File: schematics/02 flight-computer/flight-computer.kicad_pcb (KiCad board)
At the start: 2 copper layers, 186 x 186 mm, 215 parts, among them IC1 NCP4620, IC10 AD8495, IC11 AD8495, IC12 AD8656, IC13 AD8656, IC14 AD8656, IC15 AD8656, IC16 MS5611-01BA03, IC17 MPU-9250, IC18 Si4463, IC19 MAX-M8Q, IC2 STM32F405RxTx, IC20 NCP380, IC21 SN65LVDT41, IC22 MAX14787E, IC3 SL18860DC, IC4 TPS62133, IC5 ADP3335, IC6 AD8656, IC7 AD8656, IC8 AD8495, IC9 AD8495, J1 RJHSE-538x, J10 THERMO4, J11 PYRO1, J12 PYRO2, J13 PYRO_SI, J14 12V, J15 GND, J2 RJHSE-538x, J3 3V3, J4 GND, J5 PRESSURE1, J6 PRESSURE2, J7 THERMO1, J8 THERMO2, J9 THERMO3, P1 GPS, P2 TLM, P3 SWD_TC, Q1 Si5515CDC, Q2 Si5515CDC, Y1 TCXO

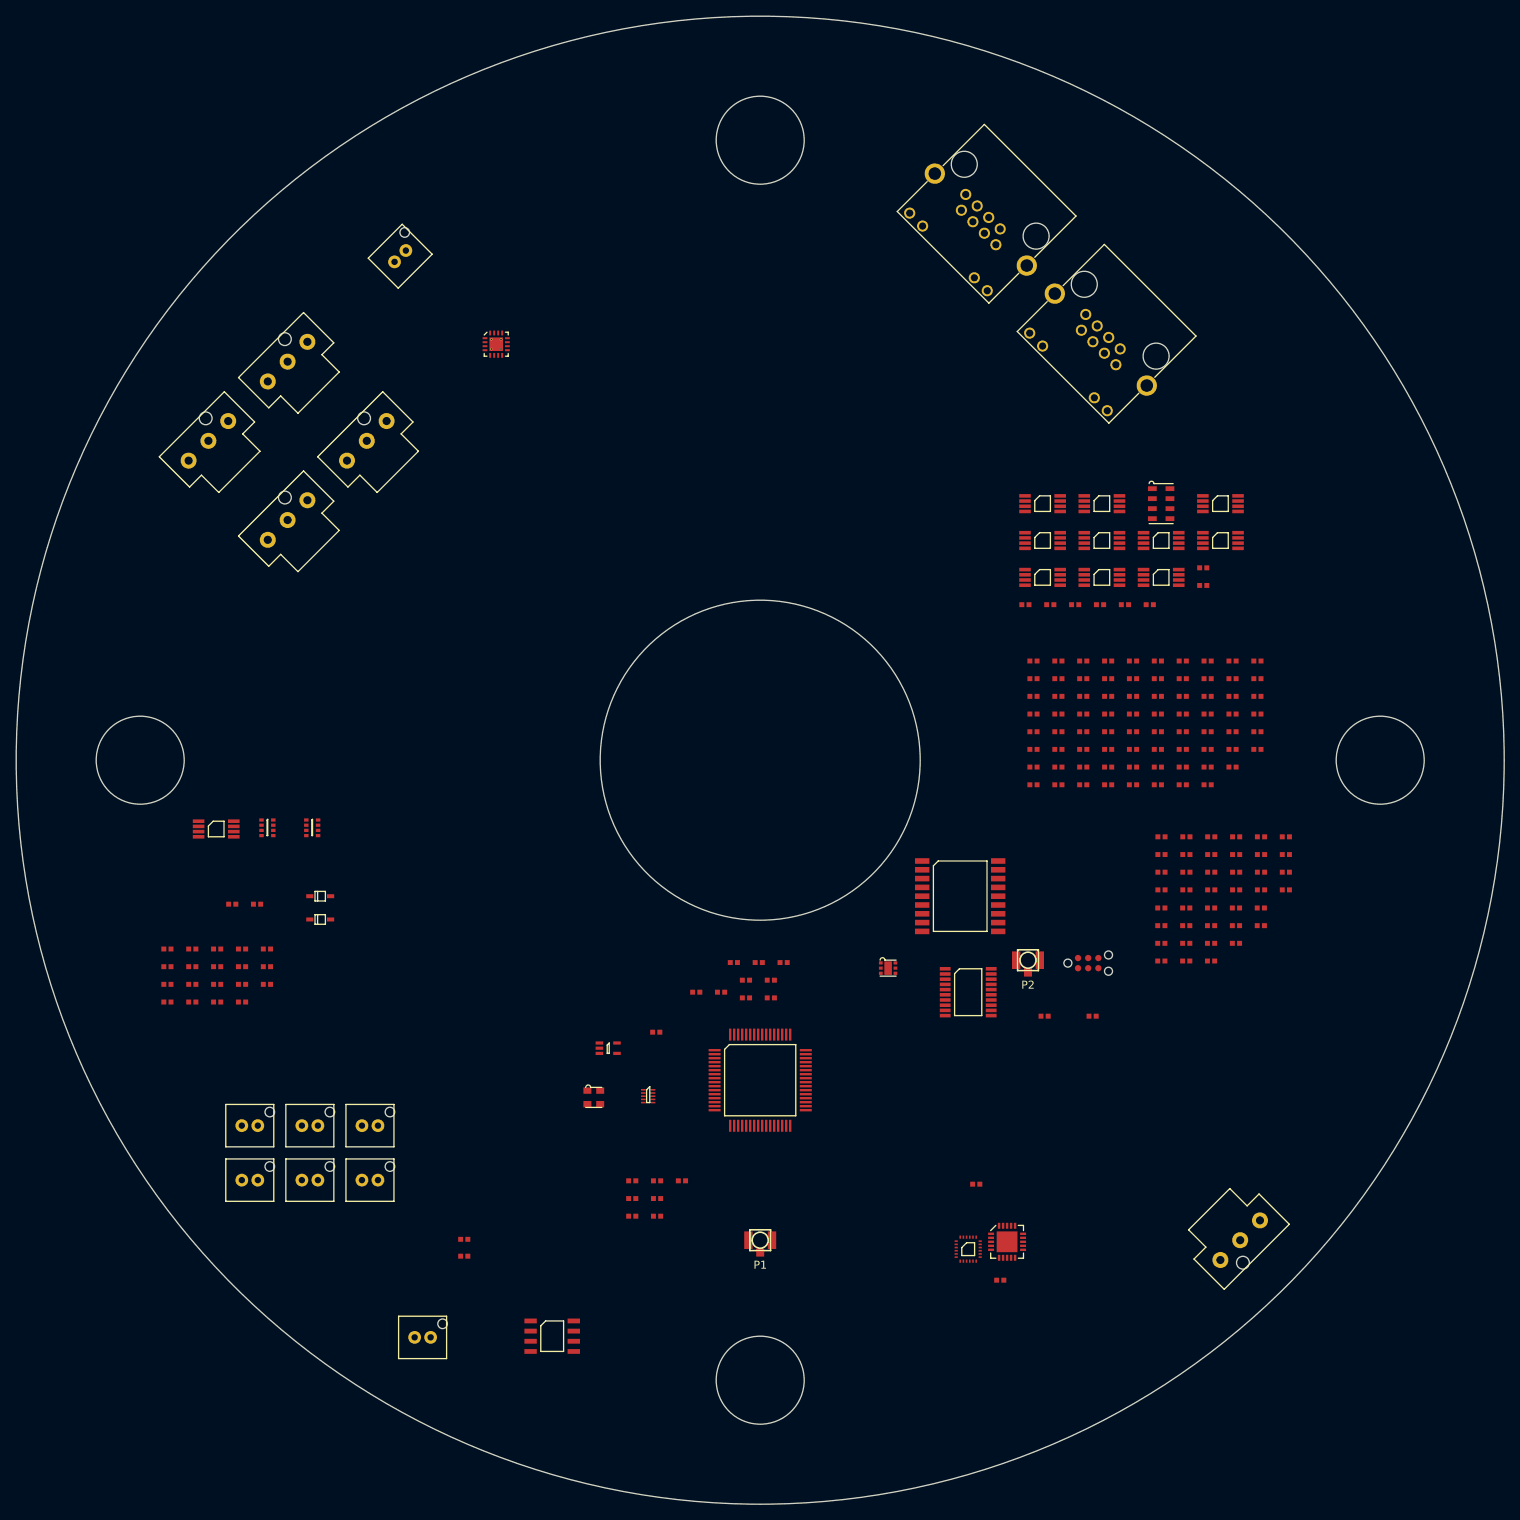
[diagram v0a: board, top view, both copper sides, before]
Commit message: Add preliminary pcb edges
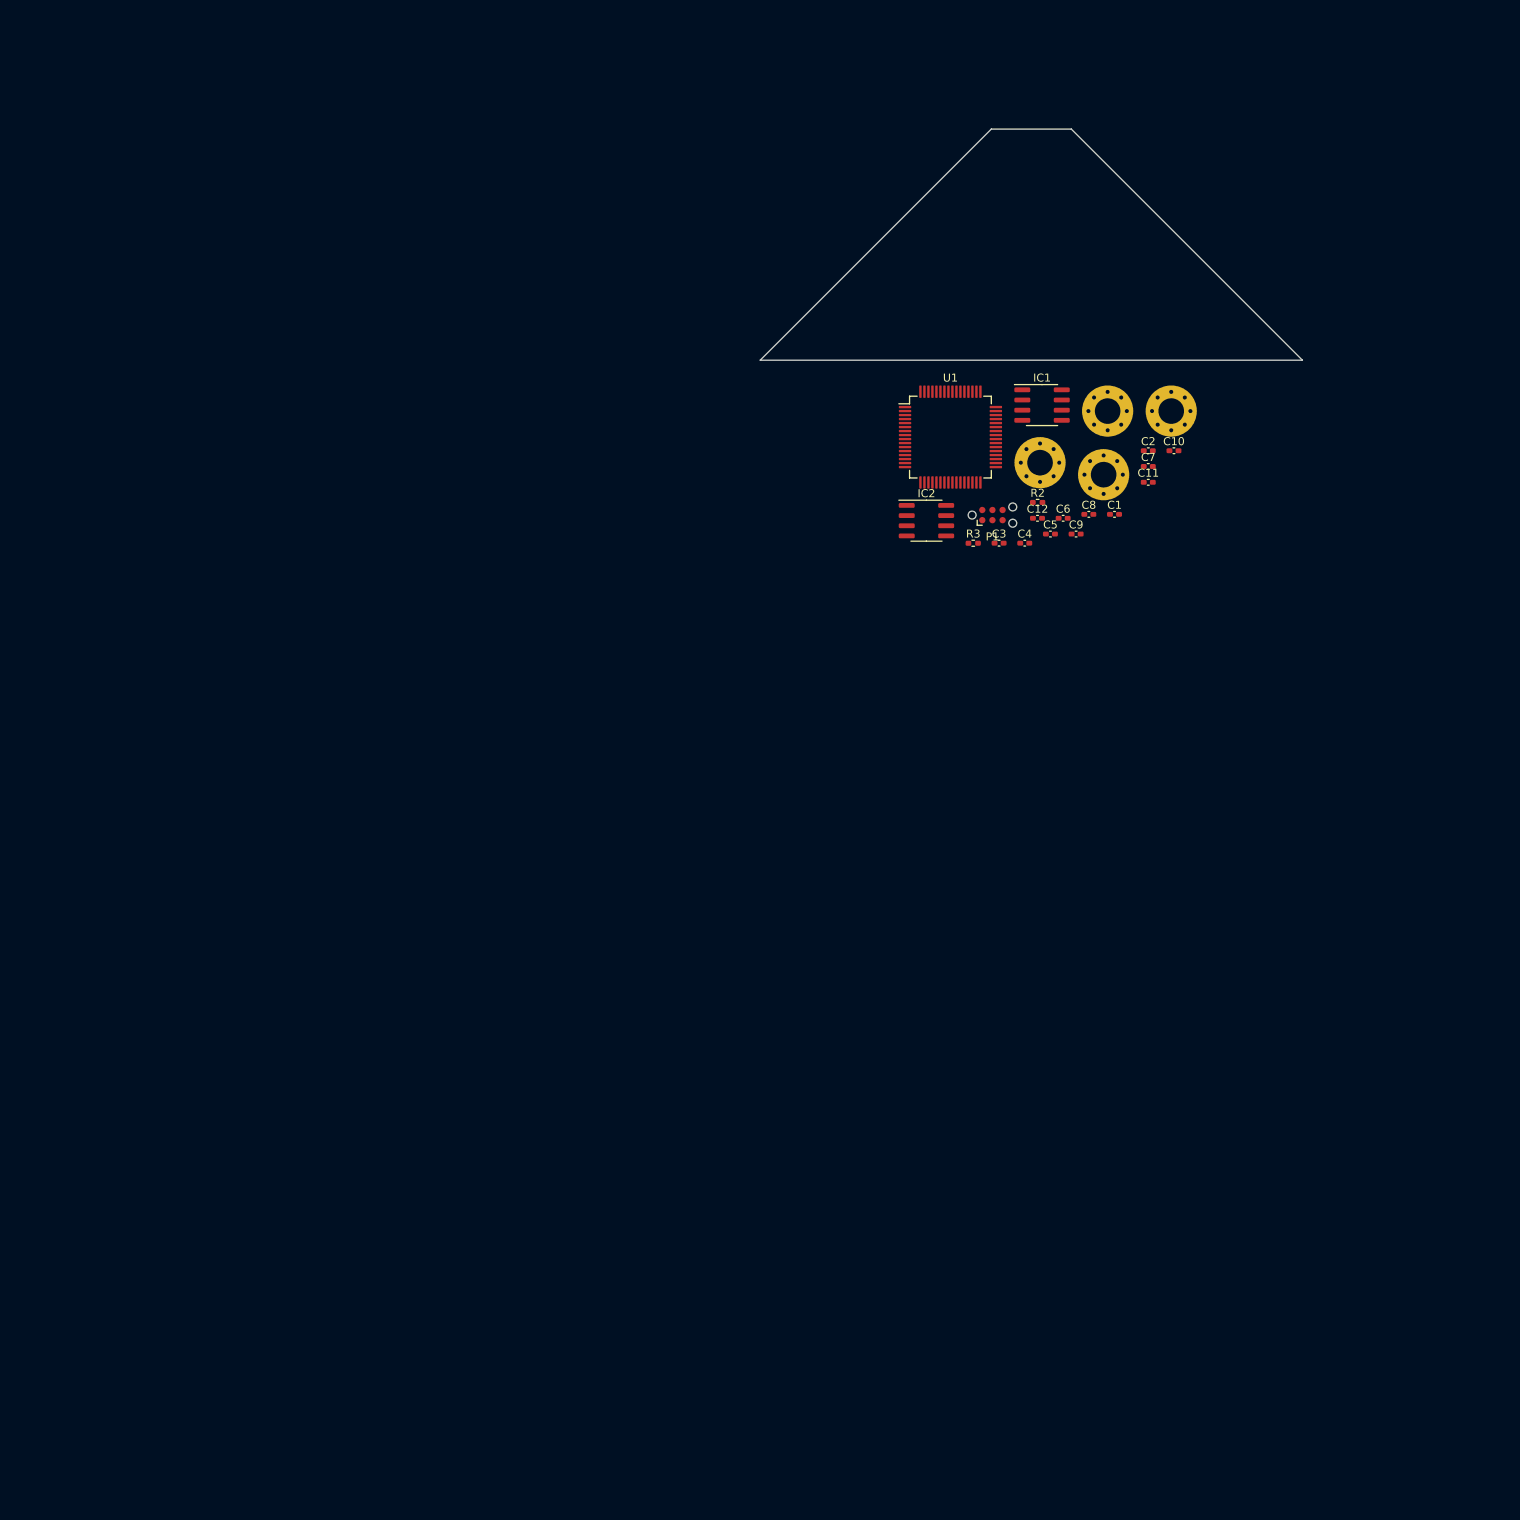
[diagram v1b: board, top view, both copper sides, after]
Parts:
- removed C13, C16, C17, C19, C20, C36, C37, C38, C39, C40, C41, C42, C43, C44, C45, C46, C47, C52, C53, C54, C55, C62, C70, C71, C84, L8: 100n, cusf:0402
- removed C14, C15: 10u, cusf:0402
- removed C18, C64: 22u, cusf:0402
- removed C21, C24, C27, C32, C33, C34, C35, C60, C63, C68, C69: 1u, cusf:0402
- removed C22, C23, C28, C29: 82n, cusf:0402
- removed C25, C26, C30, C31: 8n2, cusf:0402
- removed C48, C49, C50, C51, C56, C57, C58, C59, C61: 10n, cusf:0402
- removed C65: 200n, cusf:0402
- removed C66: 220p, cusf:0402
- removed C67: 100p, cusf:0402
- removed C72, C73: 3p, cusf:0402
- removed C74: 5p1, cusf:0402
- removed C75: 4p7, cusf:0402
- removed C76: 1p2, cusf:0402
- removed C77: 1p, cusf:0402
- removed C78: 6n8, cusf:0402
- removed C79: 6n2, cusf:0402
- removed C80, C81, C82, C83: 3p3, cusf:0402
- removed D1, D10, D11, D12, D13, D14, D2, D3, D4, D7, D8, D9: ESD_DIODE, cusf:0402
- removed D5, D6: PMEG3005AEA, cusf:SOD-323
- removed IC10, IC11, IC8, IC9: AD8495, cusf:MSOP-8
- removed IC12, IC13, IC14, IC15, IC6, IC7: AD8656, cusf:MSOP-8
- removed IC16: MS5611-01BA03, cusf:MS5611
- removed IC17: MPU-9250, cusf:QFN-24-MPU9250
- removed IC18: Si4463, cusf:QFN-20-EP-SI
- removed IC19: MAX-M8Q, cusf:MAX-M8Q
- removed IC20: NCP380, cusf:DFN-6-EP-ONSEMI
- removed IC21: SN65LVDT41, cusf:TSSOP-20
- removed IC22: MAX14787E, cusf:SOIC-8
- removed IC3: SL18860DC, cusf:DFN-10-SL18860DC
- removed IC4: TPS62133, cusf:QFN-16-EP-TI
- removed IC5: ADP3335, cusf:MSOP-8
- removed J1, J2: RJHSE-538x, cusf:RJHSE-538X
- removed J10: THERMO4, cusf:B02B-PASK
- removed J11: PYRO1, cusf:B02B-PASK
- removed J12: PYRO2, cusf:B02B-PASK
- removed J13: PYRO_SI, cusf:ULTRA-FIT-01x03
- removed J14: 12V, cusf:ULTRA-FIT-01x03
- removed J15, J4: GND, cusf:ULTRA-FIT-01x03
- removed J3: 3V3, cusf:ULTRA-FIT-01x03
- removed J5: PRESSURE1, cusf:B02B-PASK
- removed J6: PRESSURE2, cusf:B02B-PASK
- removed J7: THERMO1, cusf:B02B-PASK
- removed J8: THERMO2, cusf:B02B-PASK
- removed J9: THERMO3, cusf:B02B-PASK
- removed L1, L2: 2u2, cusf:0402
- removed L10, L12: 3n3, cusf:0402
- removed L11, L16: 24n, cusf:0402
- removed L13, L17: 22n, cusf:0402
- removed L14, L18: 12n, cusf:0402
- removed L15, L19: 11n, cusf:0402
- removed L3, L4, L5: 91n, cusf:0402
- removed L6: 120n, cusf:0402
- removed L7, L9: 18n, cusf:0402
- removed P2: TLM, cusf:uFL-R-SMT
- removed P3: SWD_TC, cusf:TC2030-NL
- removed Q1, Q2: Si5515CDC, cusf:ChipFET-1206-8
- removed R1, R10, R13, R14, R4, R5, R7, R8, R9: 10k, cusf:0402
- removed R11, R12, R25, R26, R27, R28, R29, R30, R31, R32: 1k, cusf:0402
- removed R15, R16: 150, cusf:0402
- removed R17, R18: 1k69, cusf:0402
- removed R19, R20: 6k04, cusf:0402
- removed R21, R22: 562R, cusf:0402
- removed R23, R24: 17k8, cusf:0402
- removed R33, R34, R35, R36: 1M, cusf:0402
- removed R37, R38, R39, R40: 8k87, cusf:0402
- removed R41, R42, R43, R44: 31k6, cusf:0402
- removed R45, R46, R47, R48: 2k94, cusf:0402
- removed R49, R50, R51, R52: 95k3, cusf:0402
- removed R53: 110k, cusf:0402
- removed R54: 10, cusf:0402
- removed R55: 120, cusf:0402
- removed R6: 3k3, cusf:0402
- removed Y1: TCXO, cusf:XTAL-25x20
- added H1: MountingHole_Pad, Strix:MountingHole_Pad, F.Cu at (192.9, 114.3)
- added H2: MountingHole_Pad, Strix:MountingHole_Pad, F.Cu at (201.4, 106.4)
- added H3: MountingHole_Pad, Strix:MountingHole_Pad, F.Cu at (193.4, 106.4)
- added H4: MountingHole_Pad, Strix:MountingHole_Pad, F.Cu at (185.0, 112.8)
- added U1: STM32F405RGT6, Strix:STM32F405RGT6, F.Cu at (173.8, 109.6)
- C1: value 1u -> 1µ; footprint cusf:0402 -> Strix:C_0402
- C10: value 2µ2 -> 100n; footprint cusf:0402 -> Strix:C_0402
- C11: value 1u -> 10p; footprint cusf:0402 -> Strix:C_0402
- C12: value 100n -> 10p; footprint cusf:0402 -> Strix:C_0402
- C2, C3, C4, C5, C6, C7, C9: footprint cusf:0402 -> Strix:C_0402
- C8: value 1µ -> 2µ2; footprint cusf:0402 -> Strix:C_0402
- IC1: value NCP4620 -> MAX14787E; footprint cusf:SC-70-5 -> Strix:MAX14787E
- IC2: value STM32F405RxTx -> MAX14787E; footprint cusf:LQFP-64 -> Strix:MAX14787E
- P1: value GPS -> SWD_TC; footprint cusf:uFL-R-SMT -> Strix:SWD_TC
- R2: value 10k -> 120; footprint cusf:0402 -> Strix:R_0402
- R3: value 47k -> 120; footprint cusf:0402 -> Strix:R_0402
- moved C11 112.2 mm to (198.5, 115.3)
- moved C12 97.1 mm to (184.7, 119.8)
- moved IC1 97.0 mm to (185.2, 105.6)
- moved R2 95.7 mm to (184.7, 117.8)
- moved P1 95.2 mm to (179.0, 119.4)
- moved R3 90.9 mm to (176.6, 122.9)
- moved C2 88.2 mm to (198.5, 111.3)
- moved C1 86.4 mm to (194.3, 119.3)
- moved C10 84.9 mm to (201.7, 111.3)
- moved C7 77.0 mm to (198.5, 113.3)
- moved C8 74.1 mm to (191.1, 119.3)
- moved IC2 73.0 mm to (170.8, 120.1)
- moved C6 70.0 mm to (187.9, 119.8)
- moved C4 67.8 mm to (183.1, 122.9)
- moved C9 67.6 mm to (189.5, 121.7)
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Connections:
- C1 pad 1: 3v3 -> GND
- C1 pad 2: AGND -> 3v3
- C10 pad 1: AGND -> GND
- C10 pad 2: Net-(C10-Pad2) -> /~RST
- C11 pad 1: 1v8 -> GND
- C11 pad 2: AGND -> Net-(C11-Pad2)
- C12 pad 1: 1v8 -> GND
- C12 pad 2: AGND -> (no net)
- C2 pad 1: AGND -> GND
- C3 pad 1: AGND -> GND
- C4 pad 1: AGND -> GND
- C5 pad 1: AGND -> GND
- C6 pad 1: AGND -> GND
- C7 pad 1: AGND -> GND
- C8 pad 1: AGND -> GND
- C8 pad 2: 3v3 -> Net-(C8-Pad2)
- C9 pad 1: AGND -> GND
- IC1 pad 2: (no net) -> /USART1_RX
- IC1 pad 3: AGND -> /USART1_TX
- IC1 pad 4: 1v8 -> GND
- IC1 pad 5: 3v3 -> (no net)
- IC2 pad 2: (no net) -> /UART4_RX
- IC2 pad 3: /GPS_~FLAG -> /UART4_TX
- IC2 pad 4: /GPS_~EN -> GND
- IC2 pad 5: /MCU_CLK -> (no net)
- IC2 pad 7: /~RST -> /UART4_RX-
- IC2 pad 8: /P1 -> /UART4_RX+
- P1 pad 1: /Radio/ANT_GPS -> 3v3
- P1 pad 2: AGND -> /SWDIO
- P1 pad 3: (no net) -> /~RST
- R2 pad 1: /RADIO_CLK -> /USART1_RX+
- R2 pad 2: AGND -> /USART1_RX-
- R3 pad 1: /PYRO_SI -> /UART4_RX+
- R3 pad 2: /PYRO_SI_DIV -> /UART4_RX-
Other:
- board size 186 x 186 mm -> 67.8 x 28.9 mm

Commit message: First attempt at layout
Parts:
- removed H2, H3, H4: MountingHole_Pad, Strix:MountingHole_Pad
- added J1: CONN 1 UP, Strix:TFML-110-02-L-D, F.Cu at (167.5, 95.0)
- added J2: CONN 2 UP, Strix:TFML-110-02-L-D, F.Cu at (200.5, 95.0)
- added J3: CONN 1 DOWN, Strix:SFML-110-02-L-D-LC, B.Cu at (167.5, 95.0)
- added J4: CONN 2 DOWN, Strix:SFML-110-02-L-D-LC, B.Cu at (200.5, 95.0)
- added J5: SERIAL 1, Strix:Molex_PicoBlade_53261-0871, F.Cu at (175.0, 80.0)
- added J6: SERIAL 2, Strix:Molex_PicoBlade_53261-0871, F.Cu at (193.0, 80.0)
- added R1: 100, Strix:R_0402, F.Cu at (187.4, 110.1)
- added R2: 4k7, Strix:R_0402, F.Cu at (171.8, 104.8)
- added R3: 4k7, Strix:R_0402, F.Cu at (173.3, 101.0)
- added Y1: XTAL, Strix:XTAL-20x16, F.Cu at (184.0, 111.1)
- H1: footprint Strix:MountingHole_Pad -> Strix:MountingHole_M2_Pad
- moved H1 41.5 mm to (184.0, 73.8)
- moved U1 20.8 mm to (184.0, 91.5)
- moved C1 17.6 mm to (201.5, 103.3)
- moved C12 17.6 mm to (191.9, 103.8)
- moved C3 17.6 mm to (187.1, 106.9)
- moved C4 17.6 mm to (190.3, 106.9)
- moved C5 17.6 mm to (193.5, 105.7)
- moved C6 17.6 mm to (195.1, 103.8)
- moved C8 17.6 mm to (198.3, 103.3)
- moved C9 17.6 mm to (196.7, 105.7)
- moved IC2 17.6 mm to (178.0, 104.1)
- moved P1 17.6 mm to (186.3, 103.4)
- moved R4 17.6 mm to (191.9, 101.8)
- moved R5 17.6 mm to (183.9, 106.9)
- moved C11 11.4 mm to (187.5, 112.2)
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- renumbered R2 to R4, R3 to R5
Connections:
- C12 pad 2: (no net) -> Net-(C12-Pad2)
- IC1 pad 5: (no net) -> /USART1_TX+
- IC1 pad 6: (no net) -> /USART1_TX-
- IC2 pad 5: (no net) -> /UART4_TX+
- IC2 pad 6: (no net) -> /UART4_TX-
- U1 pad 10: (no net) -> /INT_3
- U1 pad 11: (no net) -> /INT_4
- U1 pad 16: (no net) -> /GPIO_4
- U1 pad 17: (no net) -> /GPIO_5
- U1 pad 20: (no net) -> /GPIO_6
- U1 pad 21: (no net) -> /SPI1_SCLK
- U1 pad 22: (no net) -> /SPI1_MISO
- U1 pad 23: (no net) -> /SPI1_MOSI
- U1 pad 24: (no net) -> /INT_5
- U1 pad 25: (no net) -> /GPIO_7
- U1 pad 26: (no net) -> /GPIO_1
- U1 pad 27: (no net) -> /GPIO_2
- U1 pad 28: (no net) -> /GPIO_3
- U1 pad 29: (no net) -> /USART3_TX
- U1 pad 30: (no net) -> /USART3_RX
- U1 pad 34: (no net) -> /SPI2_SCLK
- U1 pad 35: (no net) -> /SPI2_MISO
- U1 pad 36: (no net) -> /SPI2_MOSI
- U1 pad 37: (no net) -> /GPIO_8
- U1 pad 38: (no net) -> /GPIO_9
- U1 pad 39: (no net) -> /GPIO_10
- U1 pad 51: (no net) -> /SPI3_SCLK
- U1 pad 52: (no net) -> /SPI3_MISO
- U1 pad 53: (no net) -> /SPI3_MOSI
- U1 pad 58: (no net) -> /I2C1_SCL
- U1 pad 59: (no net) -> /I2C1_SDA
- U1 pad 6: (no net) -> Net-(R1-Pad2)
- U1 pad 8: (no net) -> /INT_1
- U1 pad 9: (no net) -> /INT_2
